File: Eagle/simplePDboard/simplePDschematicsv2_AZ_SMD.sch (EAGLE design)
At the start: 16 parts, among them IC1 OP27Z

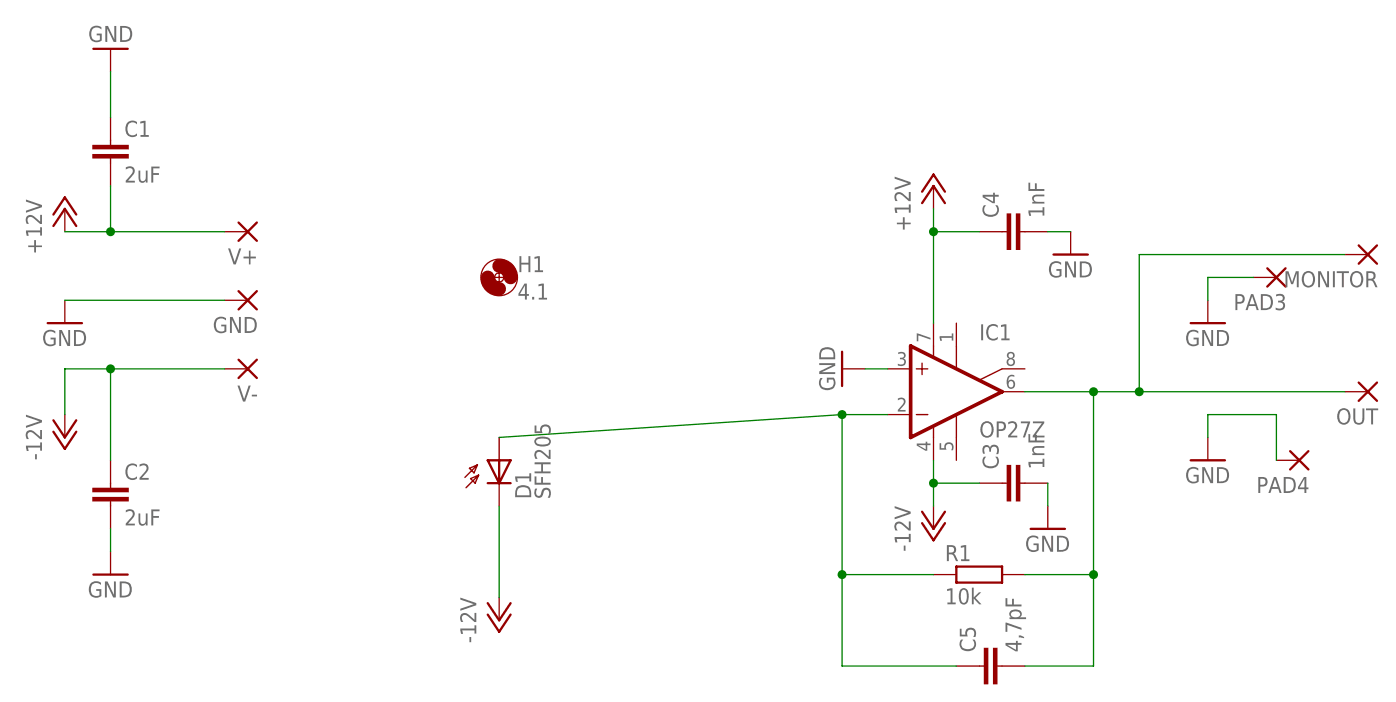
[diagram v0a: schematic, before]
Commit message: updated the PD board. PD was always properly connected. Now the symbol corresponds also to the PD we have.
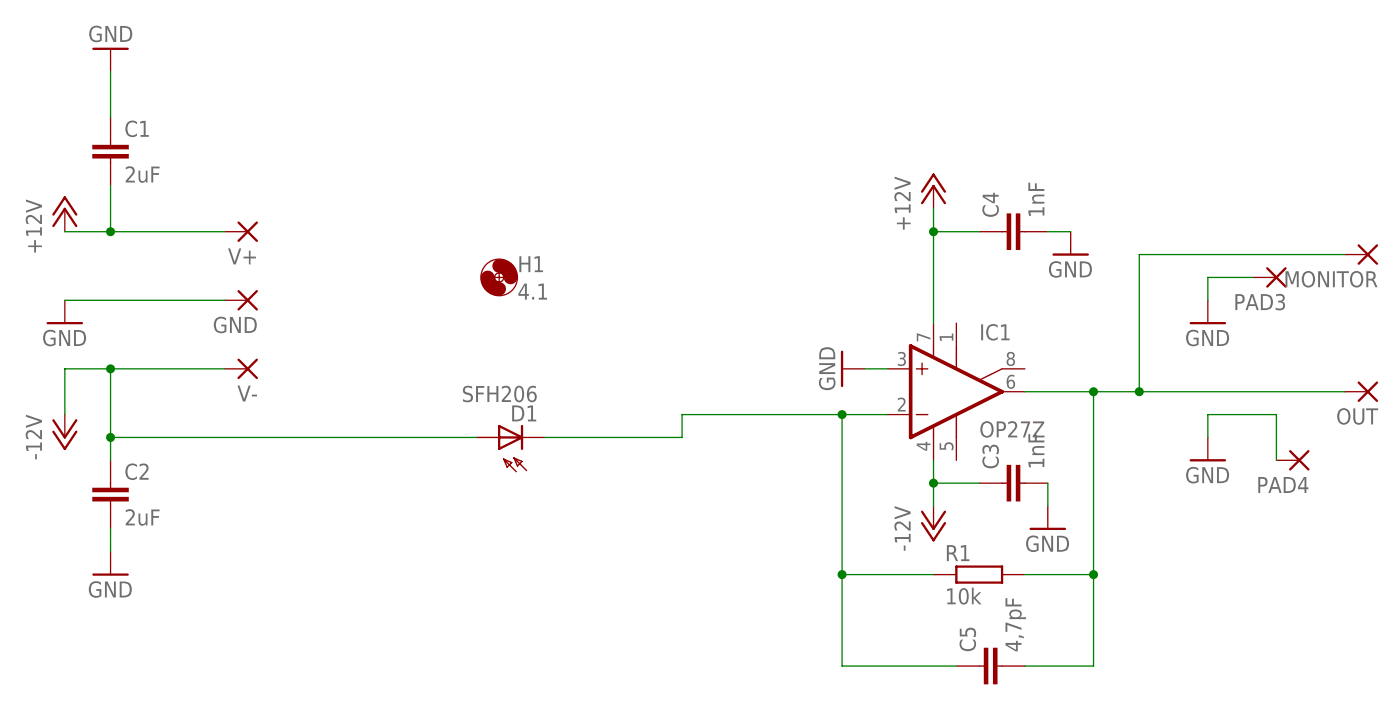
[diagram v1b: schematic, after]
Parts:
- D1: value SFH205 -> SFH206; device opto-trans-siemens:SFH205 -> opto-trans-siemens:SFH206
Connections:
- removed net N$1: C5.1, D1.A, IC1.-IN, R1.1
- new net N$3: C5.1, D1.C, IC1.-IN, R1.1
- net V-: now also D1.A; no longer D1.C
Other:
- moved on the sheet: D1
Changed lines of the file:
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@@
 </classes>
 <parts>
-<part name="D1" library="opto-trans-siemens" deviceset="SFH205" device=""/>
+<part name="D1" library="opto-trans-siemens" deviceset="SFH206" device=""/>
 <part name="IC1" library="linear" deviceset="OP27" device="Z"/>
 <part name="GND1" library="supply1" deviceset="GND" device=""/>
-<part name="P-1" library="supply1" deviceset="-12V" device=""/>
 <part name="R1" library="resistor" deviceset="R-EU_" device="M1206" value="10k"/>
 <part name="GND2" library="supply1" deviceset="GND" device=""/>
@@
 </plain>
 <instances>
-<instance part="D1" gate="1" x="106.68" y="83.82"/>
+<instance part="D1" gate="1" x="106.68" y="86.36" rot="R90"/>
 <instance part="IC1" gate="A" x="157.48" y="91.44"/>
 <instance part="GND1" gate="1" x="144.78" y="93.98" rot="R270"/>
-<instance part="P-1" gate="1" x="106.68" y="66.04"/>
 <instance part="R1" gate="G$1" x="160.02" y="71.12"/>
 <instance part="GND2" gate="1" x="185.42" y="83.82"/>
@@
 </segment>
 </net>
-<net name="N$1" class="0">
-<segment>
-<pinref part="IC1" gate="A" pin="-IN"/>
-<wire x1="144.78" y1="88.9" x2="149.86" y2="88.9" width="0.1524" layer="91"/>
-<pinref part="R1" gate="G$1" pin="1"/>
-<pinref part="C5" gate="G$1" pin="1"/>
-<wire x1="144.78" y1="88.9" x2="144.78" y2="71.12" width="0.1524" layer="91"/>
-<wire x1="144.78" y1="71.12" x2="154.94" y2="71.12" width="0.1524" layer="91"/>
-<wire x1="144.78" y1="71.12" x2="144.78" y2="60.96" width="0.1524" layer="91"/>
-<wire x1="144.78" y1="60.96" x2="157.48" y2="60.96" width="0.1524" layer="91"/>
-<junction x="144.78" y="71.12"/>
-<pinref part="D1" gate="1" pin="A"/>
-<wire x1="106.68" y1="86.36" x2="144.78" y2="88.9" width="0.1524" layer="91"/>
-<junction x="144.78" y="88.9"/>
-</segment>
-</net>
 <net name="V+" class="0">
 <segment>
@@
 </segment>
 <segment>
-<pinref part="P-1" gate="1" pin="-12V"/>
-<wire x1="106.68" y1="68.58" x2="106.68" y2="78.74" width="0.1524" layer="91"/>
-<pinref part="D1" gate="1" pin="C"/>
-</segment>
-<segment>
 <pinref part="P-3" gate="1" pin="-12V"/>
 <wire x1="63.5" y1="93.98" x2="58.42" y2="93.98" width="0.1524" layer="91"/>
 <wire x1="58.42" y1="93.98" x2="58.42" y2="88.9" width="0.1524" layer="91"/>
 <pinref part="C2" gate="G$1" pin="1"/>
-<wire x1="63.5" y1="83.82" x2="63.5" y2="93.98" width="0.1524" layer="91"/>
+<wire x1="63.5" y1="83.82" x2="63.5" y2="86.36" width="0.1524" layer="91"/>
 <junction x="63.5" y="93.98"/>
 <pinref part="V-" gate="1" pin="P"/>
+<wire x1="63.5" y1="86.36" x2="63.5" y2="93.98" width="0.1524" layer="91"/>
 <wire x1="76.2" y1="93.98" x2="63.5" y2="93.98" width="0.1524" layer="91"/>
+<pinref part="D1" gate="1" pin="A"/>
+<wire x1="104.14" y1="86.36" x2="63.5" y2="86.36" width="0.1524" layer="91"/>
+<junction x="63.5" y="86.36"/>
 </segment>
 </net>
+<net name="N$3" class="0">
+<segment>
+<pinref part="D1" gate="1" pin="C"/>
+<wire x1="111.76" y1="86.36" x2="127" y2="86.36" width="0.1524" layer="91"/>
+<pinref part="IC1" gate="A" pin="-IN"/>
+<wire x1="144.78" y1="88.9" x2="149.86" y2="88.9" width="0.1524" layer="91"/>
+<pinref part="R1" gate="G$1" pin="1"/>
+<pinref part="C5" gate="G$1" pin="1"/>
+<wire x1="144.78" y1="88.9" x2="144.78" y2="71.12" width="0.1524" layer="91"/>
+<wire x1="144.78" y1="71.12" x2="154.94" y2="71.12" width="0.1524" layer="91"/>
+<wire x1="144.78" y1="71.12" x2="144.78" y2="60.96" width="0.1524" layer="91"/>
+<wire x1="144.78" y1="60.96" x2="157.48" y2="60.96" width="0.1524" layer="91"/>
+<junction x="144.78" y="71.12"/>
+<wire x1="144.78" y1="88.9" x2="127" y2="88.9" width="0.1524" layer="91"/>
+<junction x="144.78" y="88.9"/>
+<wire x1="127" y1="86.36" x2="127" y2="88.9" width="0.1524" layer="91"/>
+</segment>
+</net>

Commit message: replaced the OP27 by a TL071 in the TI circuit
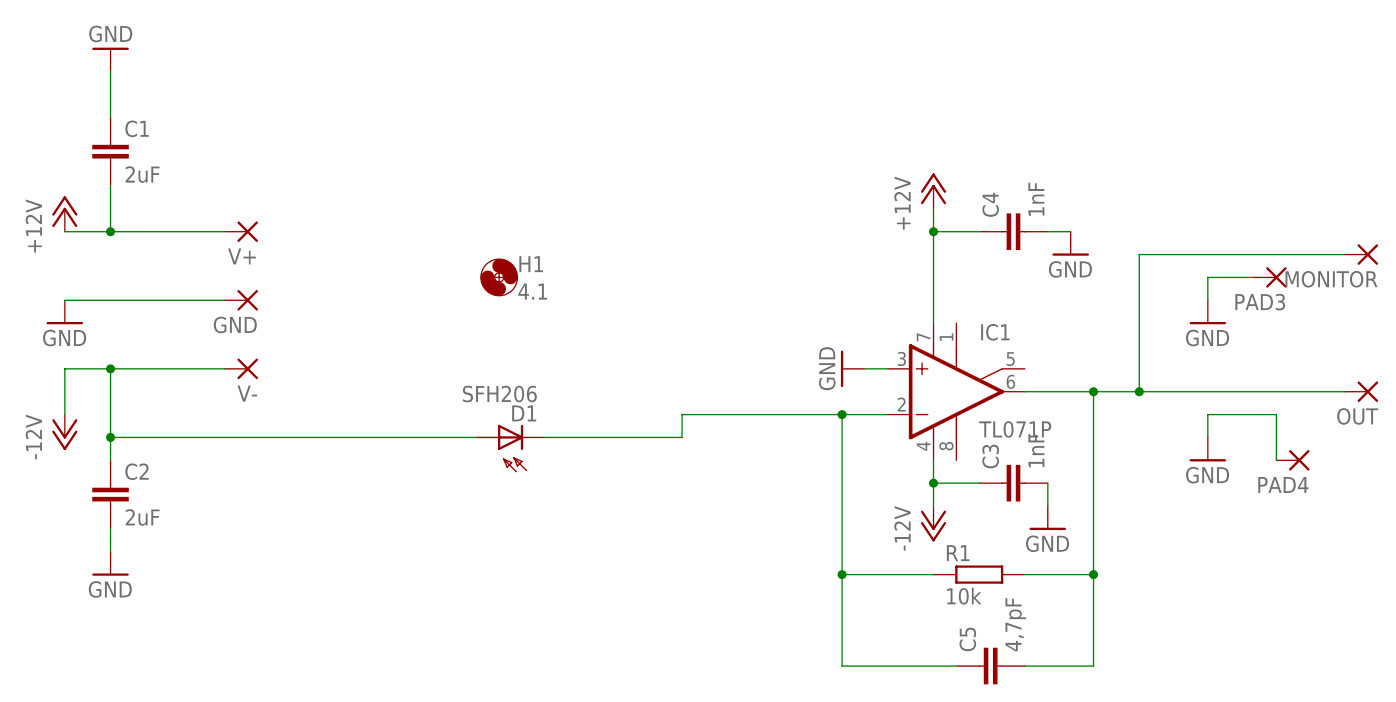
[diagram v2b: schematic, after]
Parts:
- IC1: value OP27Z -> TL071P; device linear:OP27Z -> linear:TL071P
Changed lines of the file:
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@@
 <parts>
 <part name="D1" library="opto-trans-siemens" deviceset="SFH206" device=""/>
-<part name="IC1" library="linear" deviceset="OP27" device="Z"/>
+<part name="IC1" library="linear" deviceset="TL071" device="P"/>
 <part name="GND1" library="supply1" deviceset="GND" device=""/>
 <part name="R1" library="resistor" deviceset="R-EU_" device="M1206" value="10k"/>
@@
 </sheet>
 </sheets>
-<errors>
-</errors>
 </schematic>
 </drawing>
